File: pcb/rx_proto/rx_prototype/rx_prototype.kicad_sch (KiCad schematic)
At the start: 53 parts, among them U1 nice_nano, U2 MPU-6500, U3 QMC5883P, U4 MCP6004, U5 MCP6004, U6 74HC4051

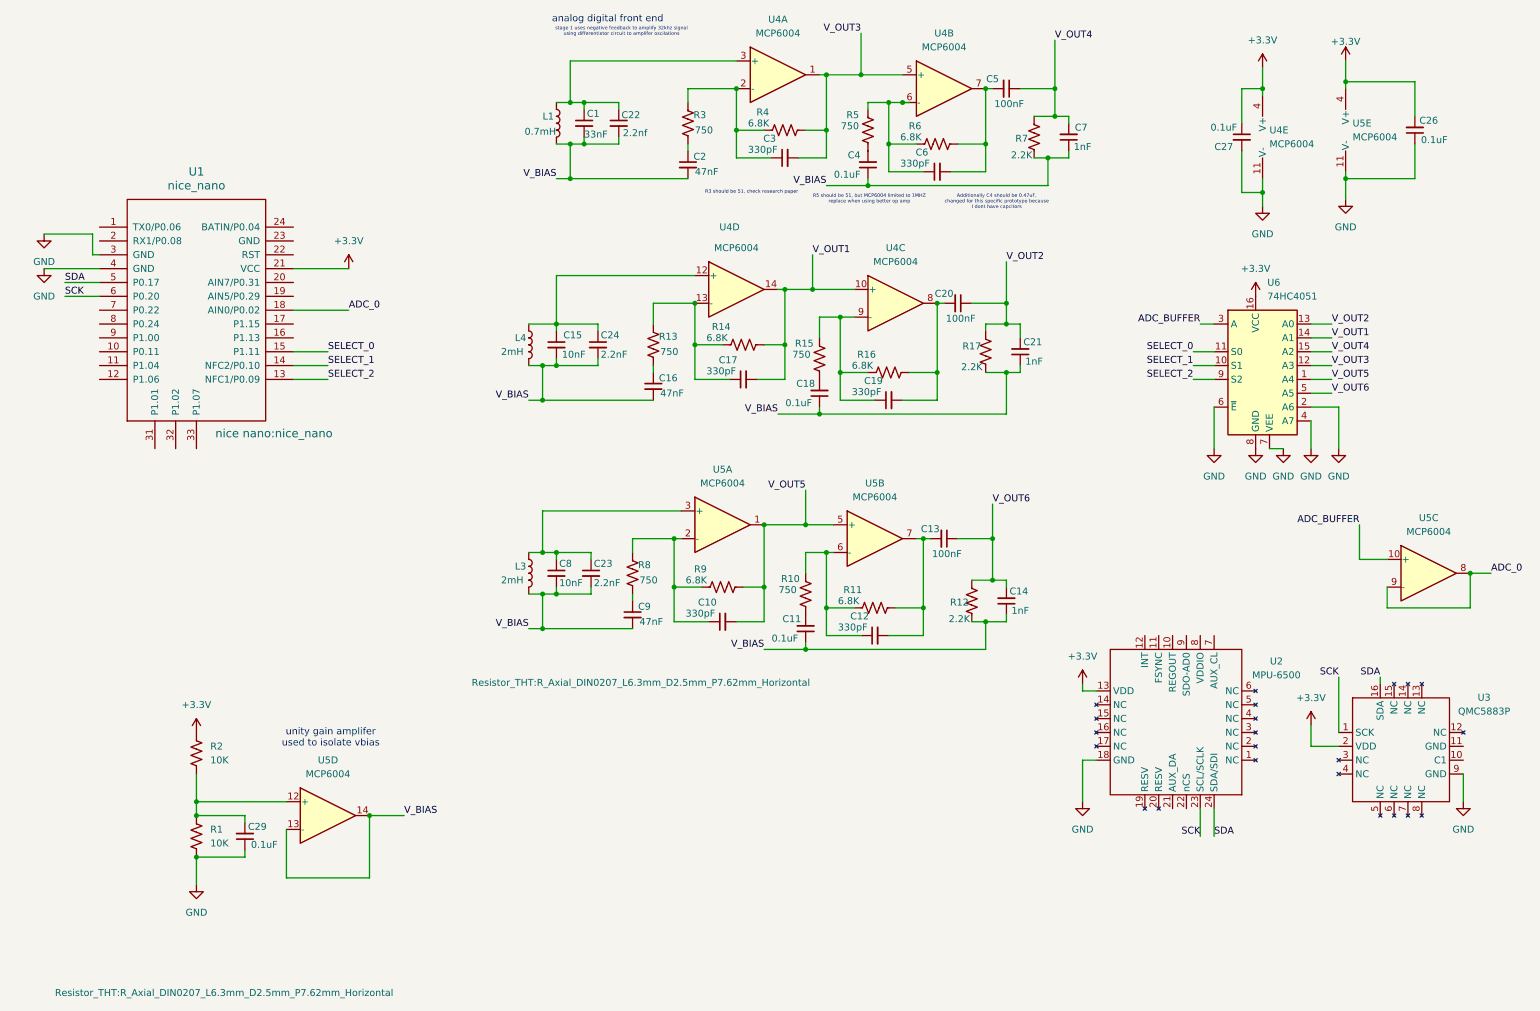
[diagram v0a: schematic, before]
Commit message: Completed perboard prototype
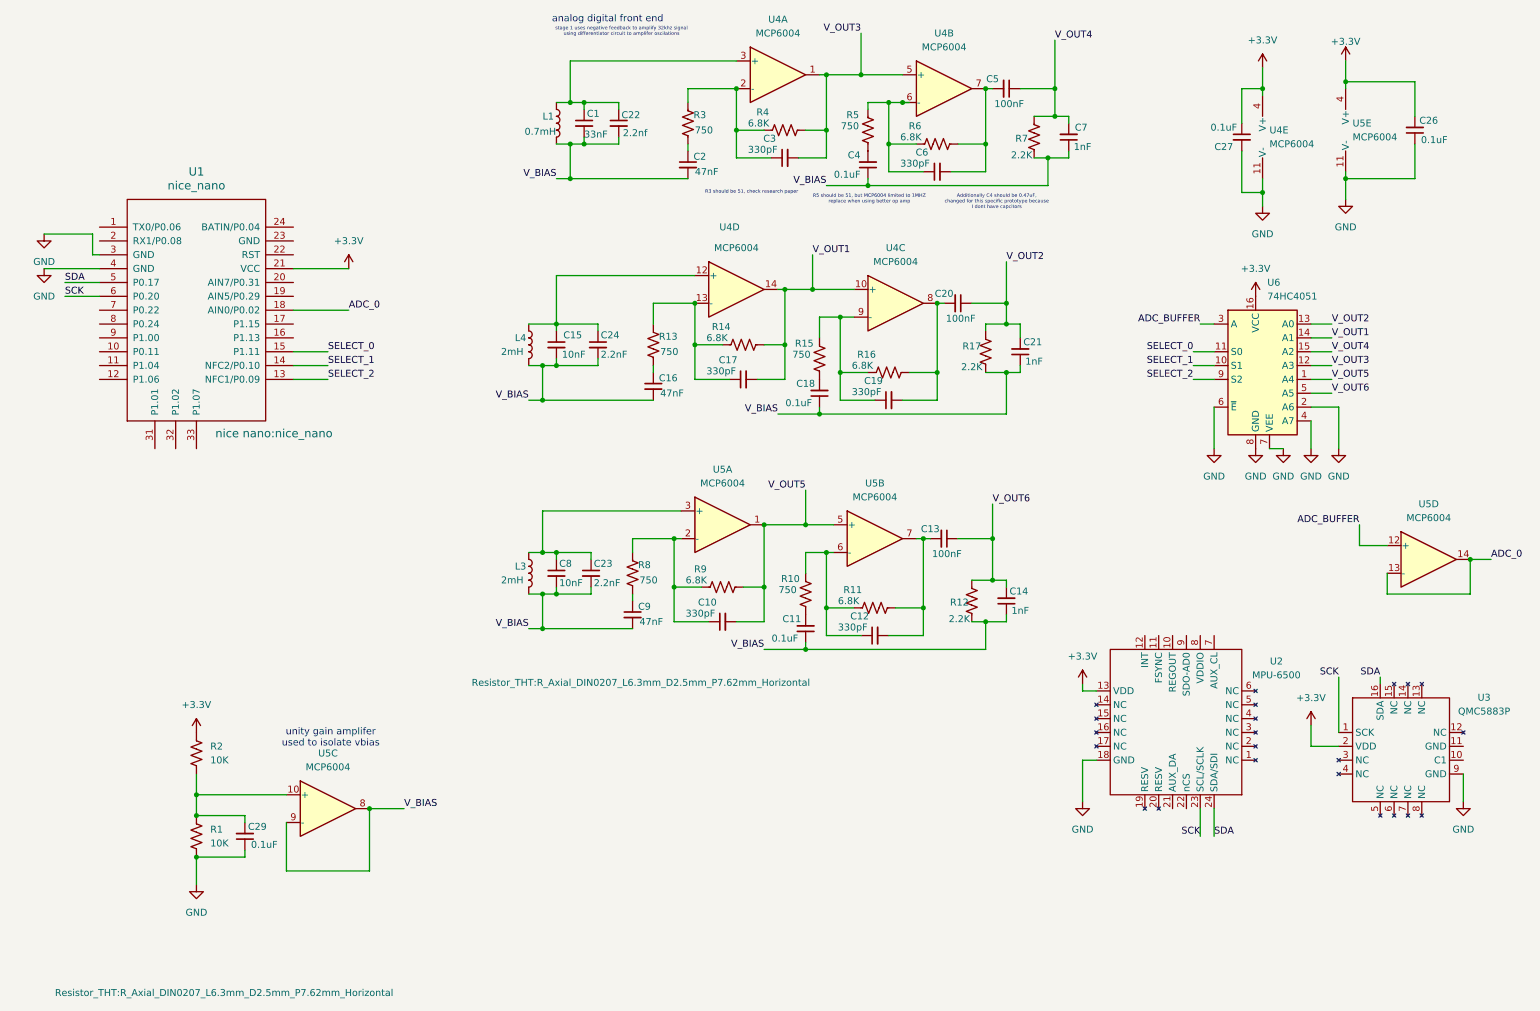
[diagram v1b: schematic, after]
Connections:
- net ADC_0: now also U5.13 (-), U5.14; no longer U5.8, U5.9 (-)
- net ADC_BUFFER: now also U5.12 (+); no longer U5.10 (+)
- net V_BIAS: now also U5.8, U5.9 (-); no longer U5.13 (-), U5.14
- net at C29.2, R1.1, R2.2: now also U5.10 (+); no longer U5.12 (+)
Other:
- moved on the sheet: U5C, U5D
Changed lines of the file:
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@@
 	)
 	(junction
-		(at 74.93 161.29)
-		(diameter 0)
-		(color 0 0 0 0)
-	)
-	(junction
 		(at 114.3 30.48)
 		(diameter 0)
@@
 	)
 	(junction
-		(at 43.18 158.75)
+		(at 74.93 160.02)
 		(diameter 0)
 		(color 0 0 0 0)
@@
 	)
 	(junction
-		(at 106.68 113.03)
+		(at 43.18 157.48)
 		(diameter 0)
 		(color 0 0 0 0)
 	)
 	(junction
-		(at 276.86 116.84)
+		(at 106.68 113.03)
 		(diameter 0)
 		(color 0 0 0 0)
@@
 	)
 	(junction
+		(at 276.86 114.3)
+		(diameter 0)
+		(color 0 0 0 0)
+	)
+	(junction
 		(at 187.96 27.94)
 		(diameter 0)
@@
 	(wire
 		(pts
+			(xy 43.18 157.48) (xy 43.18 161.29)
+		)
+		(stroke
+			(width 0)
+			(type default)
+		)
+	)
+	(wire
+		(pts
 			(xy 154.94 116.84) (xy 154.94 113.03)
 		)
@@
 	(wire
 		(pts
-			(xy 261.62 123.19) (xy 276.86 123.19)
+			(xy 261.62 120.65) (xy 276.86 120.65)
 		)
 		(stroke
@@
 	(wire
 		(pts
-			(xy 276.86 116.84) (xy 280.67 116.84)
+			(xy 276.86 114.3) (xy 280.67 114.3)
 		)
 		(stroke
@@
 	(wire
 		(pts
-			(xy 59.69 163.83) (xy 59.69 172.72)
+			(xy 59.69 162.56) (xy 59.69 171.45)
 		)
 		(stroke
@@
 	(wire
 		(pts
-			(xy 43.18 158.75) (xy 59.69 158.75)
+			(xy 43.18 157.48) (xy 59.69 157.48)
 		)
 		(stroke
@@
 	(wire
 		(pts
-			(xy 74.93 161.29) (xy 81.28 161.29)
+			(xy 74.93 160.02) (xy 81.28 160.02)
 		)
 		(stroke
@@
 	(wire
 		(pts
-			(xy 43.18 158.75) (xy 43.18 161.29)
-		)
-		(stroke
-			(width 0)
-			(type default)
-		)
-	)
-	(wire
-		(pts
-			(xy 276.86 116.84) (xy 276.86 123.19)
+			(xy 276.86 114.3) (xy 276.86 120.65)
 		)
 		(stroke
@@
 	(wire
 		(pts
-			(xy 43.18 153.67) (xy 43.18 158.75)
-		)
-		(stroke
-			(width 0)
-			(type default)
-		)
-	)
-	(wire
-		(pts
 			(xy 191.77 125.73) (xy 191.77 124.46)
 		)
@@
 	(wire
 		(pts
-			(xy 74.93 172.72) (xy 59.69 172.72)
+			(xy 74.93 171.45) (xy 59.69 171.45)
+		)
+		(stroke
+			(width 0)
+			(type default)
+		)
+	)
+	(wire
+		(pts
+			(xy 43.18 153.67) (xy 43.18 157.48)
 		)
 		(stroke
@@
 	(wire
 		(pts
-			(xy 256.54 107.95) (xy 256.54 114.3)
+			(xy 256.54 107.95) (xy 256.54 111.76)
 		)
 		(stroke
@@
 	(wire
 		(pts
-			(xy 256.54 114.3) (xy 261.62 114.3)
+			(xy 256.54 111.76) (xy 261.62 111.76)
 		)
 		(stroke
@@
 	(wire
 		(pts
-			(xy 261.62 119.38) (xy 261.62 123.19)
+			(xy 261.62 116.84) (xy 261.62 120.65)
 		)
 		(stroke
@@
 	(wire
 		(pts
-			(xy 74.93 161.29) (xy 74.93 172.72)
+			(xy 74.93 160.02) (xy 74.93 171.45)
 		)
 		(stroke
@@
 	)
 	(label "ADC_0"
-		(at 280.67 116.84 0)
+		(at 280.67 114.3 0)
 		(effects
 			(font
@@
 	)
 	(label "V_BIAS"
-		(at 81.28 161.29 0)
+		(at 81.28 160.02 0)
 		(fields_autoplaced yes)
 		(effects
@@
 		)
 		(property "voltage" "1.6"
-			(at 81.28 162.56 0)
+			(at 81.28 161.29 0)
 			(show_name no)
 			(do_not_autoplace no)
@@
 	(symbol
 		(lib_id "Amplifier_Operational:MCP6004")
-		(at 67.31 161.29 0)
+		(at 269.24 114.3 0)
 		(unit 4)
 		(body_style 1)
@@
 		(fields_autoplaced yes)
 		(property "Reference" "U5"
-			(at 67.31 151.13 0)
+			(at 269.24 104.14 0)
 			(show_name no)
 			(do_not_autoplace no)
@@
 		)
 		(property "Value" "MCP6004"
-			(at 67.31 153.67 0)
+			(at 269.24 106.68 0)
 			(show_name no)
 			(do_not_autoplace no)
@@
 		)
 		(property "Footprint" "Library:MCP6004"
-			(at 66.04 158.75 0)
+			(at 267.97 111.76 0)
 			(hide yes)
 			(show_name no)
@@
 		)
 		(property "Datasheet" "http://ww1.microchip.com/downloads/en/DeviceDoc/21733j.pdf"
-			(at 68.58 156.21 0)
+			(at 270.51 109.22 0)
 			(hide yes)
 			(show_name no)
@@
 		)
 		(property "Description" "1MHz, Low-Power Op Amp, DIP-14/SOIC-14/TSSOP-14"
-			(at 67.31 161.29 0)
+			(at 269.24 114.3 0)
 			(hide yes)
 			(show_name no)
@@
 	(symbol
 		(lib_id "Amplifier_Operational:MCP6004")
-		(at 269.24 116.84 0)
+		(at 67.31 160.02 0)
 		(unit 3)
 		(body_style 1)
@@
 		(fields_autoplaced yes)
 		(property "Reference" "U5"
-			(at 269.24 106.68 0)
+			(at 67.31 149.86 0)
 			(show_name no)
 			(do_not_autoplace no)
@@
 		)
 		(property "Value" "MCP6004"
-			(at 269.24 109.22 0)
+			(at 67.31 152.4 0)
 			(show_name no)
 			(do_not_autoplace no)
@@
 		)
 		(property "Footprint" "Library:MCP6004"
-			(at 267.97 114.3 0)
+			(at 66.04 157.48 0)
 			(hide yes)
 			(show_name no)
@@
 		)
 		(property "Datasheet" "http://ww1.microchip.com/downloads/en/DeviceDoc/21733j.pdf"
-			(at 270.51 111.76 0)
+			(at 68.58 154.94 0)
 			(hide yes)
 			(show_name no)
@@
 		)
 		(property "Description" "1MHz, Low-Power Op Amp, DIP-14/SOIC-14/TSSOP-14"
-			(at 269.24 116.84 0)
+			(at 67.31 160.02 0)
 			(hide yes)
 			(show_name no)

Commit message: Backup Prototype
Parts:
- L1, L3, L4: footprint (none) -> Connector_PinHeader_2.54mm:PinHeader_1x02_P2.54mm_Vertical
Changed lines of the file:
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@@
 			)
 		)
-		(property "Footprint" ""
+		(property "Footprint" "Connector_PinHeader_2.54mm:PinHeader_1x02_P2.54mm_Vertical"
 			(at 104.14 74.93 0)
 			(hide yes)
@@
 			)
 		)
-		(property "Footprint" ""
-			(at 104.14 116.84 0)
-			(hide yes)
+		(property "Footprint" "Connector_PinHeader_2.54mm:PinHeader_1x02_P2.54mm_Vertical"
+			(at 101.6 131.572 0)
 			(show_name no)
 			(do_not_autoplace no)
@@
 			)
 		)
-		(property "Footprint" ""
+		(property "Footprint" "Connector_PinHeader_2.54mm:PinHeader_1x02_P2.54mm_Vertical"
 			(at 109.22 34.29 0)
 			(hide yes)

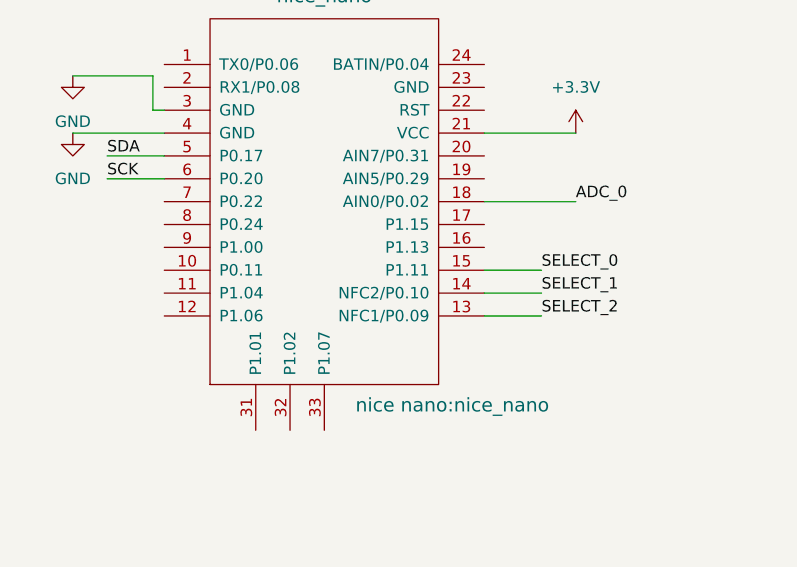
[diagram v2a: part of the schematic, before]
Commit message: Created rx board for order
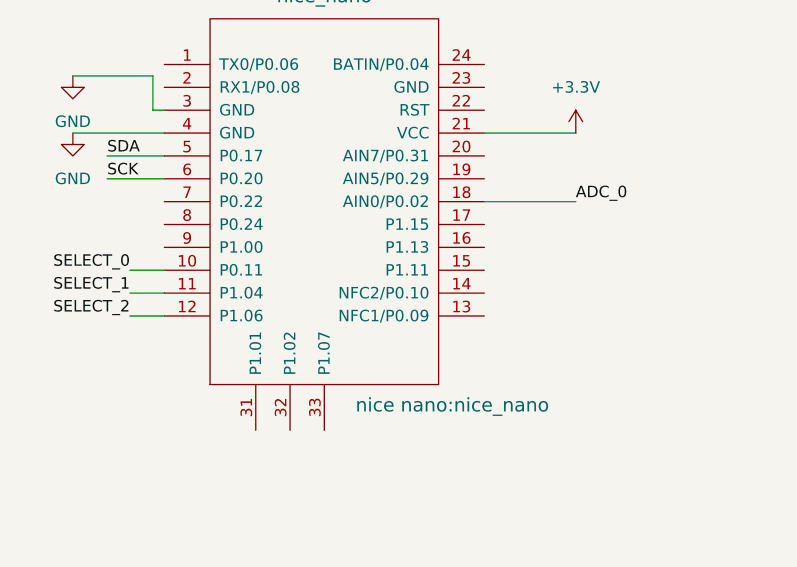
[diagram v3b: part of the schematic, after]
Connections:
- net SELECT_0: now also U1.10 (P0.11); no longer U1.15 (P1.11)
- net SELECT_1: now also U1.11 (P1.04); no longer U1.14 (NFC2/P0.10)
- net SELECT_2: now also U1.12 (P1.06); no longer U1.13 (NFC1/P0.09)
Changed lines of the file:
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@@
-	(wire
-		(pts
-			(xy 67.31 78.74) (xy 60.96 78.74)
-		)
-		(stroke
-			(width 0)
-			(type default)
-		)
-	)
 	(wire
 		(pts
@@
 	(wire
 		(pts
-			(xy 67.31 81.28) (xy 60.96 81.28)
-		)
-		(stroke
-			(width 0)
-			(type default)
-		)
-	)
-	(wire
-		(pts
 			(xy 254 43.18) (xy 254 44.45)
 		)
@@
 	(wire
 		(pts
+			(xy 21.59 81.28) (xy 25.4 81.28)
+		)
+		(stroke
+			(width 0)
+			(type default)
+		)
+	)
+	(wire
+		(pts
 			(xy 158.75 35.56) (xy 158.75 40.64)
 		)
@@
 	(wire
 		(pts
+			(xy 21.59 76.2) (xy 25.4 76.2)
+		)
+		(stroke
+			(width 0)
+			(type default)
+		)
+	)
+	(wire
+		(pts
 			(xy 227.33 160.02) (xy 227.33 165.1)
 		)
@@
 	(wire
 		(pts
+			(xy 21.59 78.74) (xy 25.4 78.74)
+		)
+		(stroke
+			(width 0)
+			(type default)
+		)
+	)
+	(wire
+		(pts
 			(xy 109.22 30.48) (xy 111.76 30.48)
 		)
@@
 		(pts
 			(xy 154.94 129.54) (xy 154.94 130.81)
-		)
-		(stroke
-			(width 0)
-			(type default)
-		)
-	)
-	(wire
-		(pts
-			(xy 67.31 76.2) (xy 60.96 76.2)
 		)
 		(stroke
@@
 	)
 	(label "SELECT_2"
-		(at 67.31 81.28 0)
-		(effects
-			(font
-				(size 1.27 1.27)
-			)
-			(justify left bottom)
+		(at 21.59 81.28 180)
+		(effects
+			(font
+				(size 1.27 1.27)
+			)
+			(justify right bottom)
 		)
 	)
@@
 	)
 	(label "SELECT_0"
-		(at 67.31 76.2 0)
-		(effects
-			(font
-				(size 1.27 1.27)
-			)
-			(justify left bottom)
+		(at 21.59 76.2 180)
+		(effects
+			(font
+				(size 1.27 1.27)
+			)
+			(justify right bottom)
 		)
 	)
@@
 	)
 	(label "SELECT_1"
-		(at 67.31 78.74 0)
-		(effects
-			(font
-				(size 1.27 1.27)
-			)
-			(justify left bottom)
-		)
-	)
+		(at 21.59 78.74 180)
+		(effects
+			(font
+				(size 1.27 1.27)
+			)
+			(justify right bottom)
+		)
+	)
